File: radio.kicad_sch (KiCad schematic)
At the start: 22 parts, among them U5 CC1101, Y2 Crystal_GND23

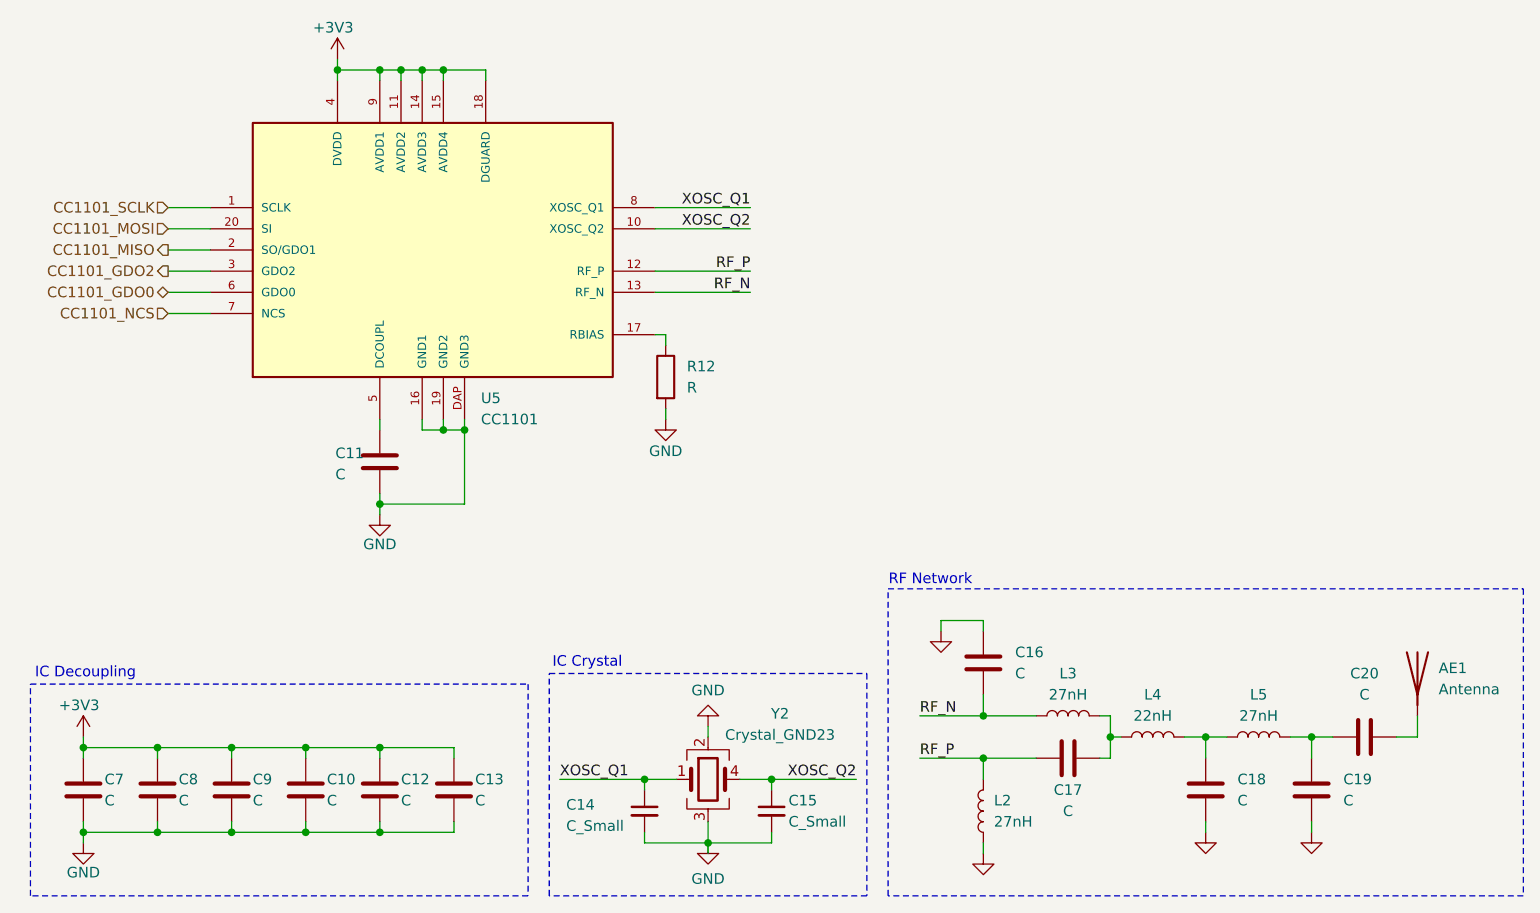
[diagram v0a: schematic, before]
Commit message: add cc1101 passives
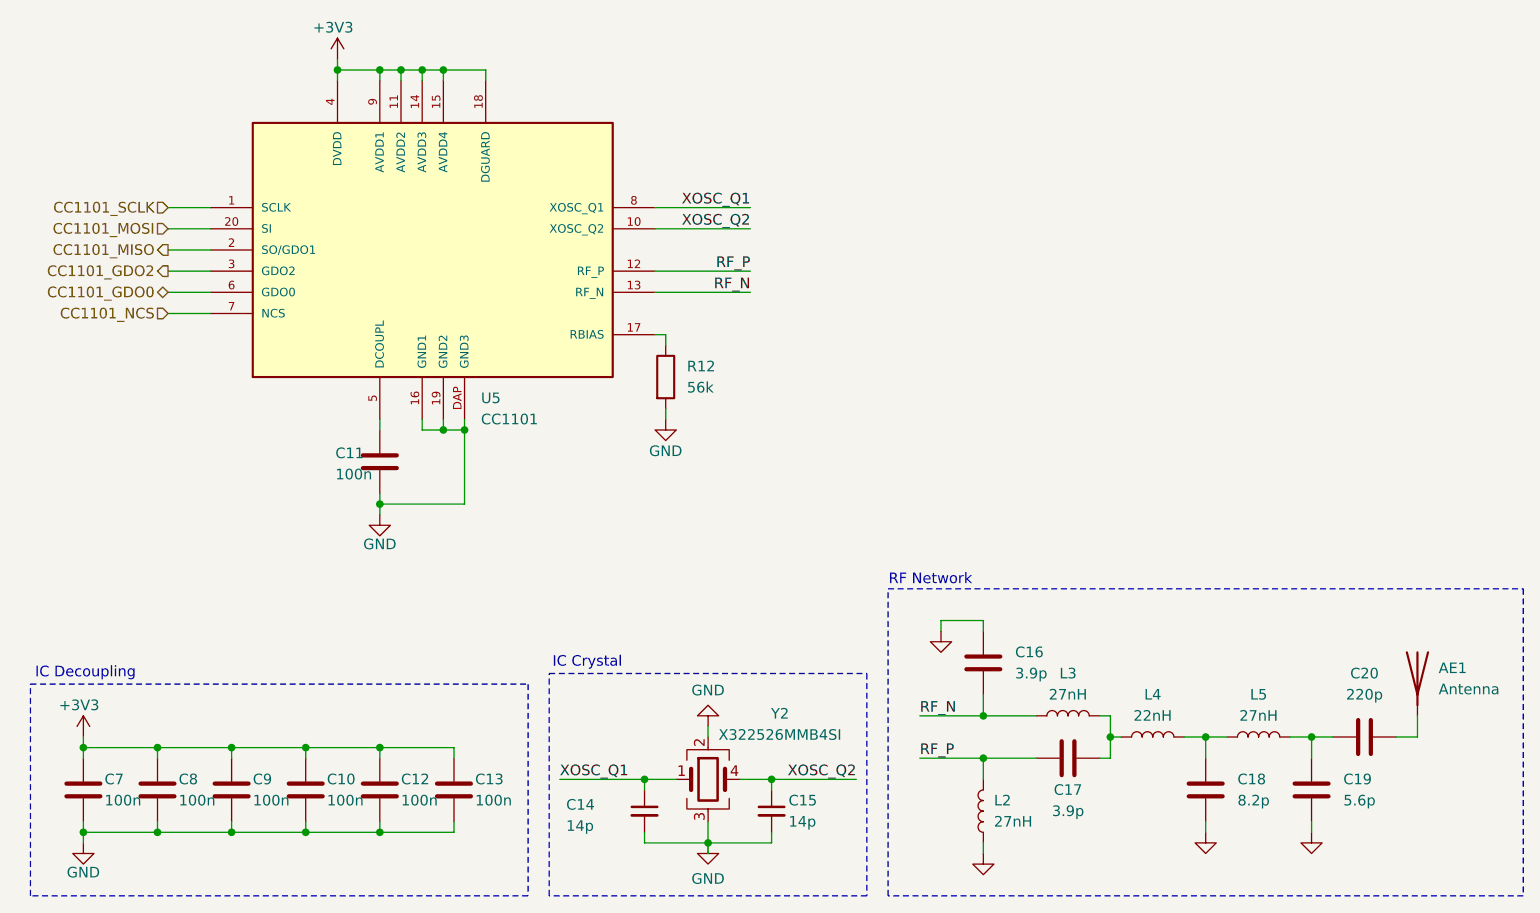
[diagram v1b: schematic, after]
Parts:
- C10, C11, C12, C13, C7, C8, C9: value C -> 100n
- C14, C15: value C_Small -> 14p
- C16, C17: value C -> 3.9p
- C18: value C -> 8.2p
- C19: value C -> 5.6p
- C20: value C -> 220p
- R12: value R -> 56k
- Y2: value Crystal_GND23 -> X322526MMB4SI
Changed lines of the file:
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@@
 			)
 		)
-		(property "Value" "C"
+		(property "Value" "100n"
 			(at 62.23 144.78 0)
 			(effects
@@
 			)
 		)
-		(property "Value" "C"
+		(property "Value" "100n"
 			(at 88.9 144.78 0)
 			(effects
@@
 			)
 		)
-		(property "Value" "C"
+		(property "Value" "3.9p"
 			(at 171.45 129.5399 0)
 			(effects
@@
 			)
 		)
-		(property "Value" "C"
+		(property "Value" "5.6p"
 			(at 210.82 144.7799 0)
 			(effects
@@
 			)
 		)
-		(property "Value" "C"
+		(property "Value" "100n"
 			(at 71.12 144.78 0)
 			(effects
@@
 			)
 		)
-		(property "Value" "C_Small"
+		(property "Value" "14p"
 			(at 117.602 147.828 0)
 			(effects
@@
 			)
 		)
-		(property "Value" "C"
+		(property "Value" "220p"
 			(at 213.36 132.08 90)
 			(effects
@@
 			)
 		)
-		(property "Value" "C_Small"
+		(property "Value" "14p"
 			(at 144.272 147.32 0)
 			(effects
@@
 			)
 		)
-		(property "Value" "R"
+		(property "Value" "56k"
 			(at 132.08 95.2499 0)
 			(effects
@@
 			)
 		)
-		(property "Value" "C"
+		(property "Value" "8.2p"
 			(at 198.12 144.7799 0)
 			(effects
@@
 			)
 		)
-		(property "Value" "C"
+		(property "Value" "100n"
 			(at 80.01 144.78 0)
 			(effects
@@
 			)
 		)
-		(property "Value" "C"
+		(property "Value" "100n"
 			(at 97.79 144.78 0)
 			(effects
@@
 			)
 		)
-		(property "Value" "Crystal_GND23"
+		(property "Value" "X322526MMB4SI"
 			(at 143.256 136.906 0)
 			(effects
@@
 			)
 		)
-		(property "Value" "C"
+		(property "Value" "100n"
 			(at 89.916 105.664 0)
 			(effects
@@
 			)
 		)
-		(property "Value" "C"
+		(property "Value" "3.9p"
 			(at 177.8 146.05 90)
 			(effects
@@
 			)
 		)
-		(property "Value" "C"
+		(property "Value" "100n"
 			(at 106.68 144.78 0)
 			(effects
